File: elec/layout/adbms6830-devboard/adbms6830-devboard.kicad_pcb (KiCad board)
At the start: 2 copper layers, 239 parts

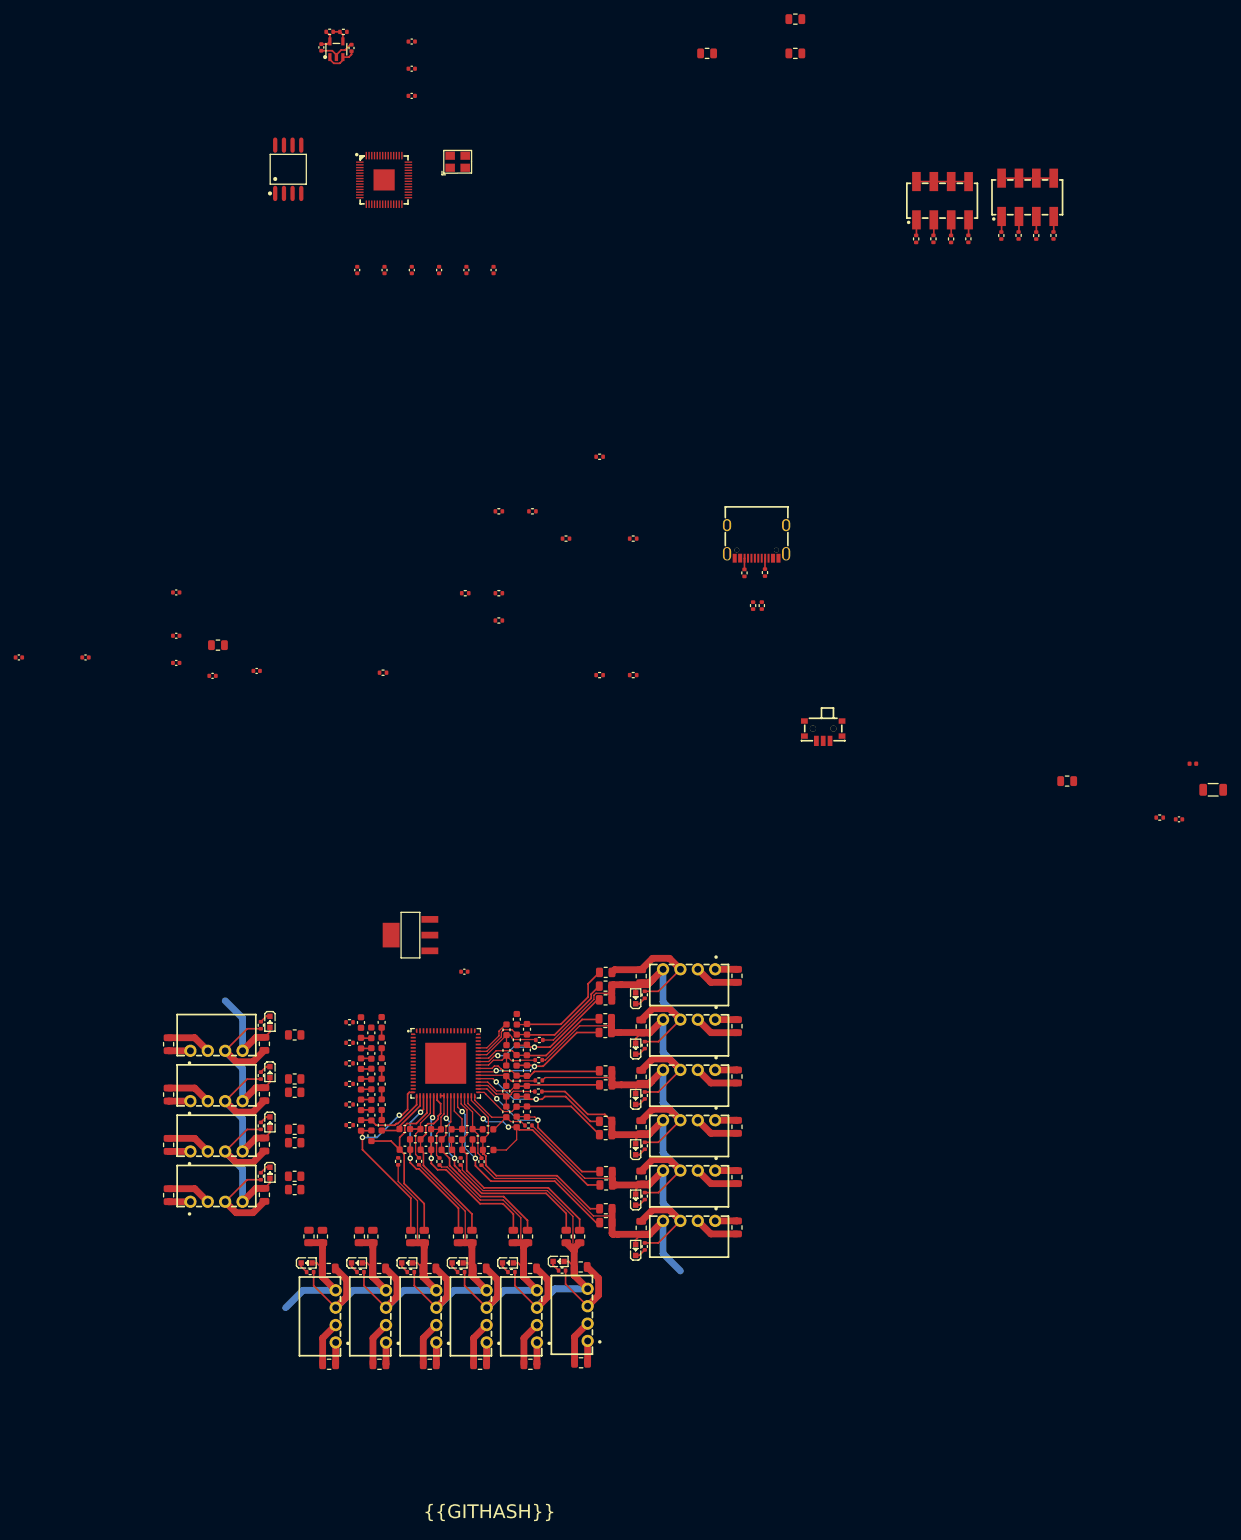
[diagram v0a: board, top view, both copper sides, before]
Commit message: add isospi connector
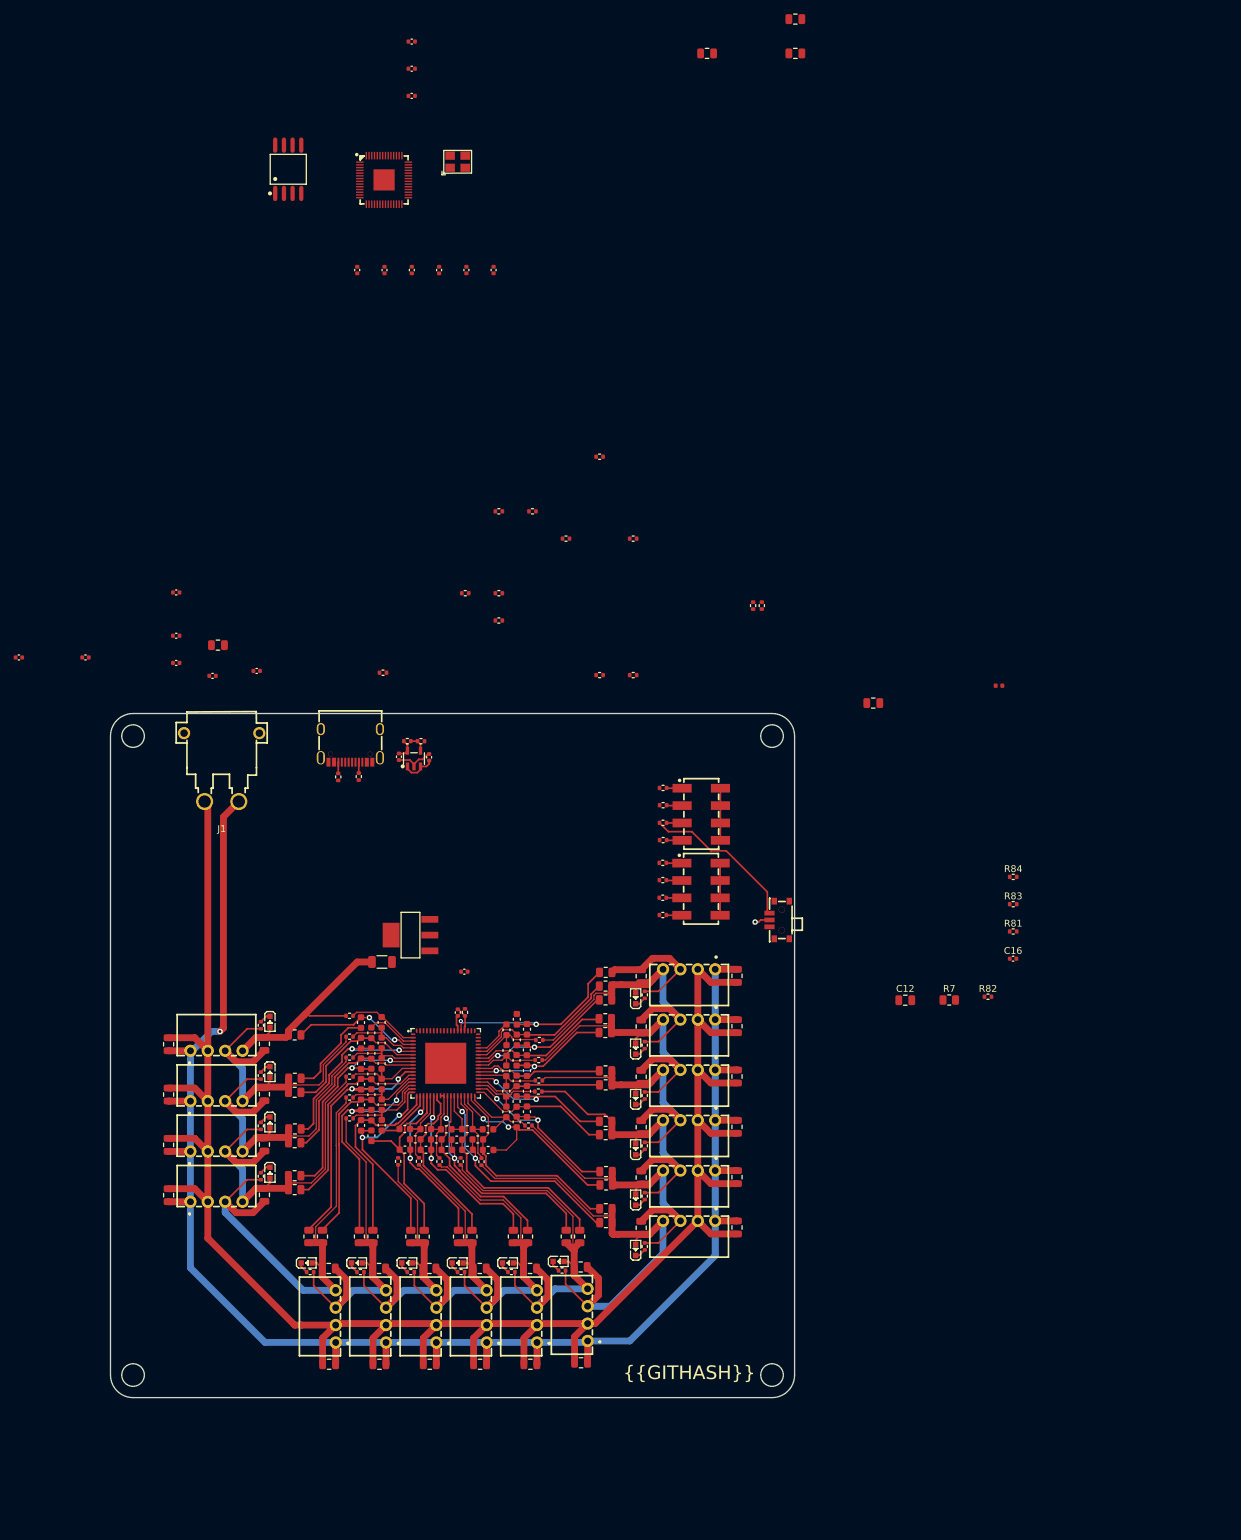
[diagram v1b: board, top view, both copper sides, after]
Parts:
- added C12: 50V 10nF X7R ±10% 0805 Multilayer Ceramic Capacitors MLCC -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, lib:C0805, F.Cu at (161.9, 95.8)
- added C16: 16V 100nF X7R ±10% 0402 Multilayer Ceramic Capacitors MLCC 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, lib:C0402, F.Cu at (177.7, 89.7)
- added J1: , lib:CONN-TH_XT30PW-M, F.Cu at (62.0, 61.7)
- added R7: 125mW Thick Film Resistors 150V ±100ppm/℃ ±1% 1kΩ 0805 Chip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, lib:R0805, F.Cu at (168.3, 95.7)
- added R81: 62.5mW Thick Film Resistors 50V ±1% ±200ppm/℃ 1Ω 0402 Chip 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, lib:R0402, F.Cu at (177.7, 85.7)
- added R82: 62.5mW Thick Film Resistors 50V ±1% ±200ppm/℃ 1Ω 0402 Chip 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, lib:R0402, F.Cu at (174.0, 95.2)
- added R83: 62.5mW Thick Film Resistors 50V ±1% ±200ppm/℃ 1Ω 0402 Chip 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, lib:R0402, F.Cu at (177.7, 81.7)
- added R84: 62.5mW Thick Film Resistors 50V ±1% ±200ppm/℃ 1Ω 0402 Chip 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, lib:R0402, F.Cu at (177.7, 77.7)
- moved R5 124.1 mm to (85.4, 90.2), turned to 0 degrees
- moved C8 109.1 mm to (96.5, 97.6), turned to -90 degrees
- moved R96 108.5 mm to (126.5, 83.3), turned to 0 degrees
- moved U25 106.7 mm to (132.0, 79.5), turned to -90 degrees
- moved R6 105.5 mm to (97.5, 97.5), turned to -90 degrees
- moved R92 105.2 mm to (126.5, 72.4), turned to 0 degrees
- moved R95 105.1 mm to (126.4, 80.8), turned to 0 degrees
- moved C106 104.3 mm to (92.3, 60.2)
- moved C107 104.3 mm to (87.9, 60.2)
- moved R87 104.3 mm to (89.1, 57.9)
- moved R88 104.3 mm to (91.1, 57.9)
- moved U23 104.3 mm to (90.1, 60.4)
- moved U24 102.0 mm to (132.1, 68.6), turned to -90 degrees
- moved R94 101.7 mm to (126.5, 78.2), turned to 0 degrees
- moved R91 101.7 mm to (126.5, 69.8), turned to 0 degrees
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- renumbered C98 to C100, C99 to C101, C100 to C102, C101 to C103, C102 to C104, C103 to C105, C104 to C106, C105 to C107, C12 to C13, C13 to C14, C14 to C15, C15 to C17, C16 to C18, C17 to C19, C18 to C20, C19 to C21, C20 to C22, C21 to C23, C22 to C24, C23 to C25, C24 to C26, C25 to C27, C26 to C28, C27 to C29, C28 to C30, C29 to C31, C30 to C32, C31 to C33, C32 to C34, C33 to C35, C34 to C36, C35 to C37, C36 to C38, C37 to C39, C38 to C40, C39 to C41, C40 to C42, C41 to C43, C42 to C44, C43 to C45, C44 to C46, C45 to C47, C46 to C48, C47 to C49, C48 to C50, C49 to C51, C50 to C52, C51 to C53, C52 to C54, C53 to C55, C54 to C56, C55 to C57, C56 to C58, C57 to C59, C58 to C60, C59 to C61, C60 to C62, C61 to C63, C62 to C64, C63 to C65, C64 to C66, C65 to C67, C66 to C68, C67 to C69, C68 to C70, C69 to C71, C70 to C72, C71 to C73, C72 to C74, C73 to C75, C74 to C76, C75 to C77, C76 to C78, C77 to C79, C78 to C80, C79 to C81, C80 to C82, C81 to C83, C82 to C84, C83 to C85, C84 to C86, C85 to C87, C86 to C88, C87 to C89, C88 to C90, C89 to C91, C90 to C92, C91 to C93, C92 to C94, C93 to C95, C94 to C96, C95 to C97, C96 to C98, C97 to C99, R9 to R10, R10 to R11, R11 to R12, R12 to R13, R13 to R14, R14 to R15, R15 to R16, R16 to R17, R17 to R18, R18 to R19, R19 to R20, R20 to R21, R21 to R22, R22 to R23, R23 to R24, R24 to R25, R25 to R26, R26 to R27, R27 to R28, R28 to R29, R29 to R30, R30 to R31, R31 to R32, R32 to R33, R33 to R34, R34 to R35, R35 to R36, R36 to R37, R37 to R38, R38 to R39, R39 to R40, R40 to R41, R41 to R42, R42 to R43, R43 to R44, R44 to R45, R45 to R46, R46 to R47, R47 to R48, R48 to R49, R49 to R50, R50 to R51, R51 to R52, R52 to R53, R53 to R54, R54 to R55, R55 to R56, R56 to R57, R57 to R58, R58 to R59, R59 to R60, R60 to R61, R61 to R62, R62 to R63, R63 to R64, R64 to R65, R65 to R66, R66 to R67, R67 to R68, R68 to R69, R69 to R70, R70 to R71, R71 to R72, R72 to R73, R73 to R74, R74 to R75, R75 to R76, R76 to R77, R77 to R78, R78 to R79, R7 to R8, R79 to R80, R80 to R85, R81 to R86, R82 to R87, R83 to R88, R84 to R89, R8 to R9, R85 to R90, R86 to R91, R87 to R92, R88 to R93, R89 to R94, R90 to R95, R91 to R96
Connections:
- R77 pad 2: micro-cs -> micro-cs-1
- R93 pad 1: mosi -> bms.ic-mosi
- R94 pad 1: miso -> bms.ic-miso
- U1 pad 54: mosi -> bms.ic-mosi
- U1 pad 57: miso -> bms.ic-miso
- U19 pad 11: miso -> micro-miso
- U19 pad 12: bms.ic-cs -> micro-cs
- U19 pad 13: bms.ic-sck -> micro-sck
- U19 pad 14: mosi -> micro-mosi
- U19 pad 52: micro-sck -> micro-sck-1
- U19 pad 56: micro-cs -> micro-cs-1
- U21 pad 1: micro-cs -> micro-cs-1
- U21 pad 6: micro-sck -> micro-sck-1
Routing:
- net cell_sim-gnd: track 51.1 -> 253.2 mm, vias 0 -> 1
- net cell_sim-vcc: track 104.3 -> 288.3 mm
- net bms.cell12-gnd: track 34.2 -> 71.4 mm
- net s13n: track 1.53 -> 37.5 mm, vias 0 -> 2
- net s12n: track 1.53 -> 35.0 mm, vias 0 -> 2
- net s14n: track 1.53 -> 32.7 mm, vias 0 -> 2
- net s12p: track 1.53 -> 32.0 mm
- net s13p: track 1.52 -> 29.6 mm
- net bms.cell13-gnd: track 27.8 -> 55.7 mm
- net s15n: track 1.53 -> 27.7 mm, vias 0 -> 2
- net s14p: track 1.53 -> 25.1 mm
- net bms.cell14-gnd: track 27.8 -> 51.1 mm
- net bms.ic-vcc-1: track 0.00 -> 23.2 mm
- net bms.cell15-gnd: track 27.8 -> 48.6 mm
- net s16n: track 0.00 -> 20.7 mm
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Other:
- board outline added: 100 x 100 mm

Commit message: layout complete
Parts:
- added U20: , lib:KEY-SMD_4P-L4.2-W3.2-P2.20-LS4.6, F.Cu at (134.7, 82.4)
- added U21: , lib:KEY-SMD_4P-L4.2-W3.2-P2.20-LS4.6, F.Cu at (119.7, 67.7)
- added U24: , lib:CONN-SMD_2P-P2.00_MOLEX_5023520201, F.Cu at (175.2, 58.0)
- added U25: , lib:CONN-SMD_2P-P2.00_MOLEX_5023520201, F.Cu at (158.2, 57.9)
- moved C95 129.2 mm to (123.4, 84.4), turned to 90 degrees
- moved C100 125.9 mm to (122.8, 77.1), turned to 180 degrees
- moved C101 118.9 mm to (134.2, 73.8)
- moved C2 116.7 mm to (176.3, 64.4), turned to 90 degrees
- moved C1 115.5 mm to (173.8, 64.4), turned to 90 degrees
- moved C6 115.0 mm to (145.1, 91.9)
- moved U22 114.9 mm to (126.0, 84.2), turned to 180 degrees
- moved C4 109.6 mm to (156.8, 64.3), turned to 90 degrees
- moved U19 109.4 mm to (128.8, 76.4)
- moved U23 108.5 mm to (127.1, 67.6), turned to -90 degrees
- moved C5 107.8 mm to (159.3, 64.3), turned to 90 degrees
- moved C3 102.5 mm to (154.0, 90.6), turned to 90 degrees
- moved C94 101.3 mm to (126.0, 81.9), turned to 180 degrees
- moved C104 99.8 mm to (128.8, 71.1), turned to 90 degrees
- moved C96 99.0 mm to (134.2, 77.5), turned to 0 degrees
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- renumbered U20 to U22, U21 to U23, U22 to U26, U23 to U27, U24 to U28, U25 to U29
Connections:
- C100 pad 2: bms-gnd-1 -> bms.ic-gnd
- C101 pad 2: bms-gnd-1 -> bms.ic-gnd
- C102 pad 2: bms-gnd-1 -> bms.ic-gnd
- C103 pad 2: bms-gnd-1 -> bms.ic-gnd
- C104 pad 2: bms-gnd-1 -> bms.ic-gnd
- C105 pad 2: bms-gnd-1 -> bms.ic-gnd
- C106 pad 2: bms-gnd-1 -> bms.ic-gnd
- C107 pad 2: bms-gnd-1 -> bms.ic-gnd
- C12 pad 2: bms-gnd-1 -> bms.ic-gnd
- C4 pad 1: bms.ic-p -> ipb
- C4 pad 2: bms.ic-p -> bms-p-1
- C5 pad 1: bms.ic-n -> imb
- C5 pad 2: bms.ic-n -> bms-n-1
- C63 pad 2: bms-gnd-1 -> bms.ic-gnd
- C7 pad 2: bms-gnd-1 -> bms.ic-gnd
- C94 pad 2: bms-gnd-1 -> bms.ic-gnd
- C95 pad 2: bms-gnd-1 -> bms.ic-gnd
- C96 pad 2: bms-gnd-1 -> bms.ic-gnd
- C97 pad 2: bms-gnd-1 -> bms.ic-gnd
- C98 pad 2: bms-gnd-1 -> bms.ic-gnd
- C99 pad 2: bms-gnd-1 -> bms.ic-gnd
- R10 pad 1: bms-gnd-1 -> bms.ic-gnd
- R2 pad 2: bms-p -> bms.ic-cs
- R3 pad 1: bms.ic-p -> ipb
- R4 pad 2: bms.ic-p -> imb
- R56 pad 1: bms.ic-vcc -> bms.ic-vcc-2
- R58 pad 1: bms.ic-vcc -> bms.ic-vcc-2
- R60 pad 2: bms-gnd-1 -> bms.ic-gnd
- R85 pad 2: bms-gnd-1 -> bms.ic-gnd
- R86 pad 2: bms-gnd-1 -> bms.ic-gnd
- R88 pad 2: bms-gnd-1 -> bms.ic-gnd
- R93 pad 1: bms.ic-mosi -> micro-mosi
- R94 pad 1: bms.ic-miso -> micro-miso
- R95 pad 1: bms.ic-sck -> micro-sck
- R96 pad 1: bms.ic-cs -> micro-cs
- U1 pad 55: bms.ic-n -> imb
- U1 pad 56: bms.ic-p -> ipb
- U19 pad 19: bms-gnd-1 -> bms.ic-gnd
- U19 pad 57: bms-gnd-1 -> bms.ic-gnd
- U22 pad 2: bms-gnd-1 -> bms.ic-gnd
- U22 pad 4: bms-gnd-1 -> bms.ic-gnd
- U23 pad 4: bms-gnd-1 -> bms.ic-gnd
- U26 pad 1: bms-gnd-1 -> bms.ic-gnd
- U26 pad 2: bms-gnd-1 -> bms.ic-gnd
- U26 pad 3: bms-gnd-1 -> bms.ic-gnd
- U26 pad 4: bms-gnd-1 -> bms.ic-gnd
- U26 pad A1: bms-gnd-1 -> bms.ic-gnd
- U26 pad A12: bms-gnd-1 -> bms.ic-gnd
- U26 pad B1: bms-gnd-1 -> bms.ic-gnd
- U26 pad B12: bms-gnd-1 -> bms.ic-gnd
- U27 pad 2: bms-gnd-1 -> bms.ic-gnd
- U28 pad 2: bms_ref_debug.header-gnd -> bms.ic-gnd
- U28 pad 4: bms_ref_debug.header-gnd -> bms.ic-gnd
- U28 pad 6: bms_ref_debug.header-gnd -> bms.ic-gnd
- U28 pad 8: bms_ref_debug.header-gnd -> bms.ic-gnd
- U29 pad 2: bms-gnd -> bms.ic-gnd
- U29 pad 4: bms-gnd -> bms.ic-gnd
- U29 pad 6: bms-gnd -> bms.ic-gnd
- U29 pad 8: bms-gnd -> bms.ic-gnd
- U3 pad 3: bms-gnd-1 -> bms.ic-gnd
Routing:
- net micro-vcc: track 3.05 -> 74.5 mm, vias 0 -> 6
- net bms.ic-vcc-2: track 0.00 -> 69.6 mm, vias 0 -> 6
- net bms.ic-gnd: track 2.33 -> 70.2 mm, vias 0 -> 42
- net bms.ic-vcc-1: track 23.2 -> 90.6 mm, vias 0 -> 3
- net bms.ic-vcc: track 0.00 -> 65.3 mm, vias 0 -> 2
- net micro-cs: track 0.00 -> 61.8 mm, vias 0 -> 3
- net micro-sck: track 0.00 -> 59.6 mm, vias 0 -> 3
- net bms.ic-cs: track 0.00 -> 47.0 mm
- net isomd: track 2.58 -> 49.4 mm, vias 1 -> 2
- net io: track 3.67 -> 49.7 mm, vias 0 -> 2
- net bms.ic-sck: track 0.00 -> 44.9 mm
- net imb: track 0.00 -> 38.0 mm
- net ipb: track 0.00 -> 37.7 mm
- net micro-mosi: track 0.00 -> 34.1 mm, vias 0 -> 3
- net micro-miso: track 0.00 -> 31.2 mm, vias 0 -> 2
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- added copper zone on B.Cu, net bms.ic-gnd
- added copper zone on F.Cu, net bms.ic-gnd
- added copper zone on In1.Cu, net bms.ic-gnd
- added copper zone on In2.Cu, net bms.ic-gnd
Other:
- outline, holes or cut-outs redrawn
- copper layers 2 -> 4
- board text added: "cs"
- board text added: "miso"
- board text added: "mosi"
- board text added: "sck"
- board text added: "vref2"
- board text added: "vreg"
